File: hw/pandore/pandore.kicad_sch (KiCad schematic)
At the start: 17 parts

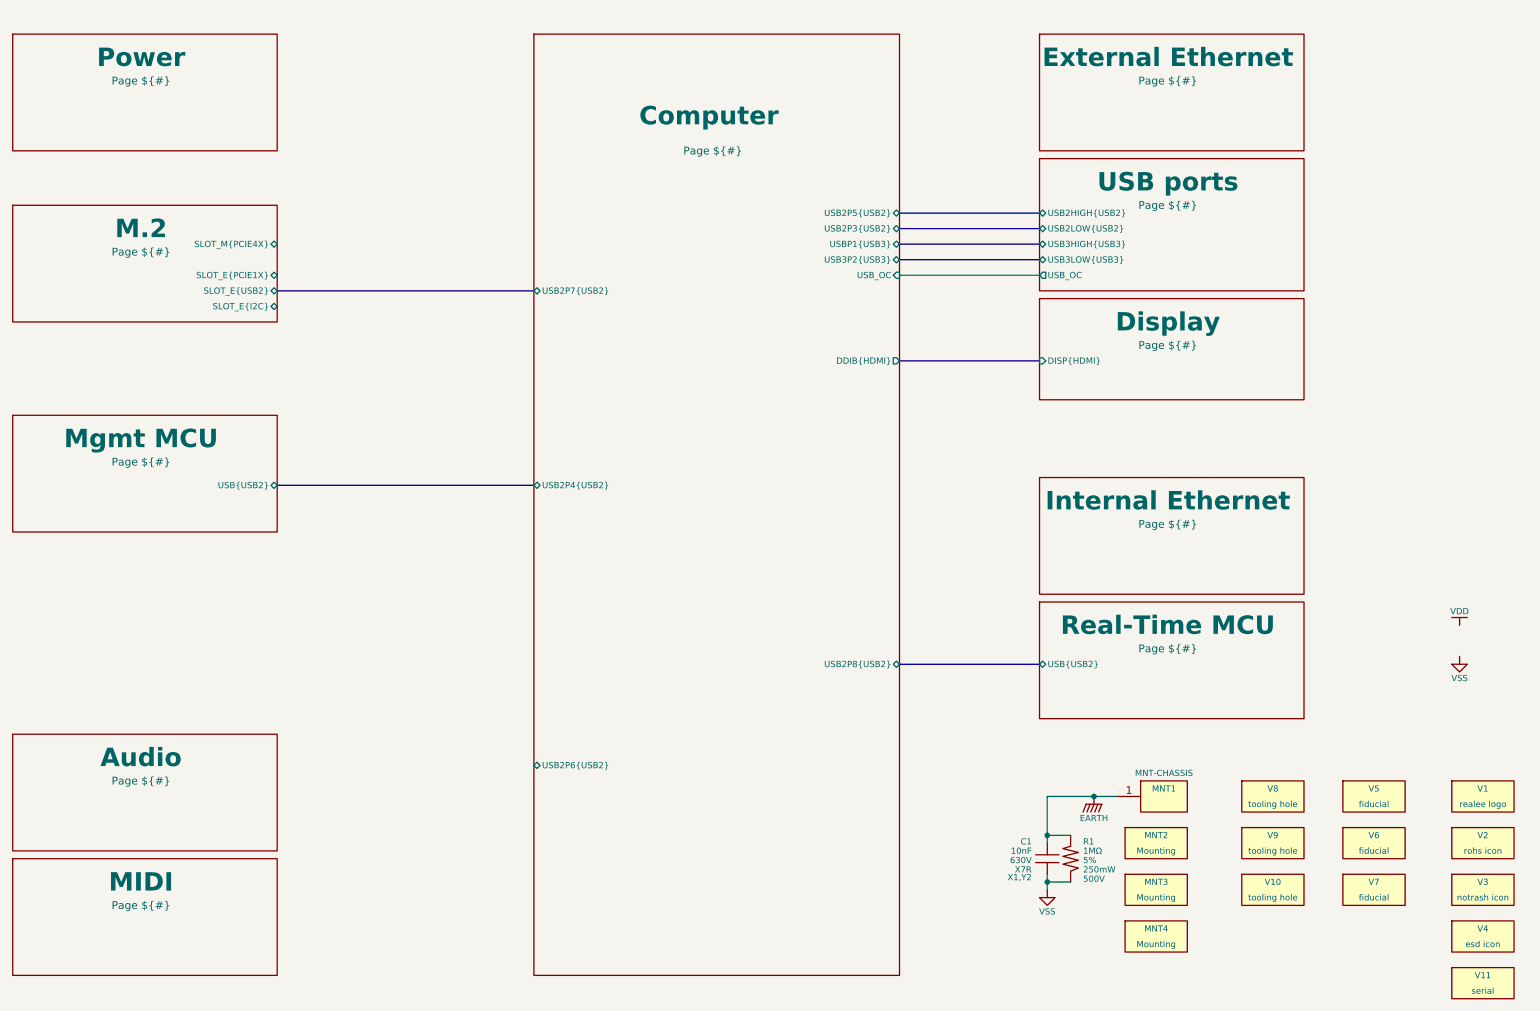
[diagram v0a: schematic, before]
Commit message: added usb, hdmi and combo xlrtrs connectors resized pcb for something realistic (still wip)
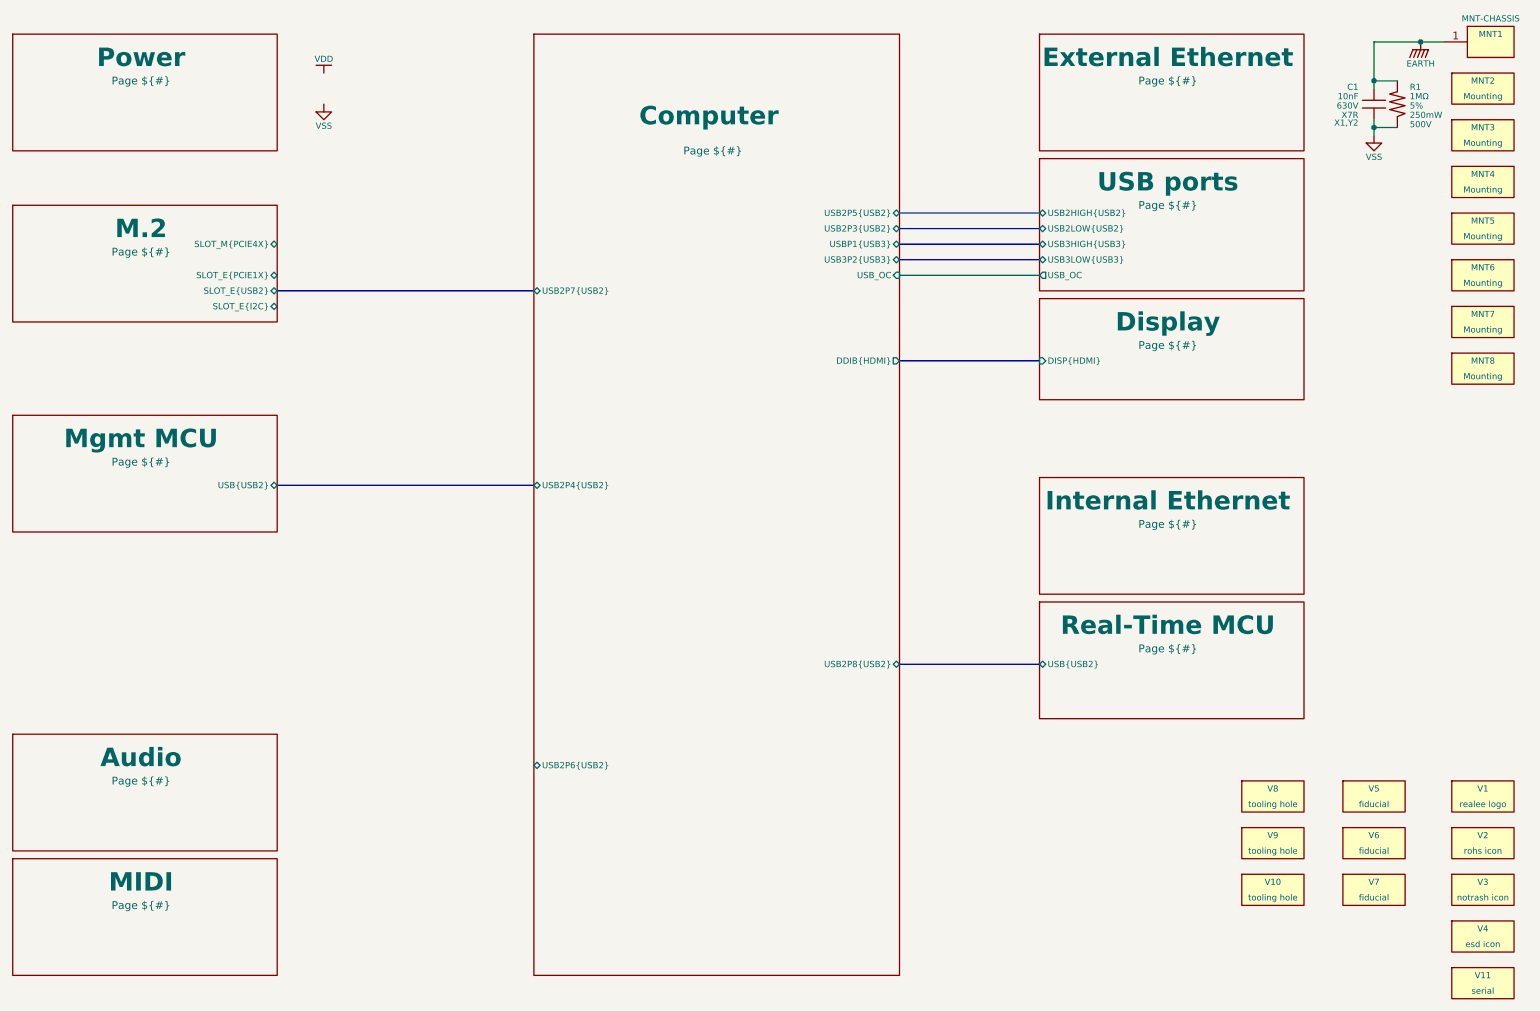
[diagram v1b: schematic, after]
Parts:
- added MNT5, MNT6, MNT7, MNT8: Mounting, reekilib_mnt:mnt_M3, symbol reekilib_vrt:virtual
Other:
- moved on the sheet: C1, MNT1, MNT2, MNT3, MNT4, R1

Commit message: Added lots to sch and pcb: eth passive, audio codec, midi, teensy Corrected and added support for M.2
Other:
- sheet Audio ports: added MIDI{UART}, USB{USB2}; removed none
- sheet Computer ports: added ETHI{PCIE1X}, ETHX{PCIE1X}, M2E{PCIE1X}, M2M{PCIE4X}, MIDI{UART}; removed none
- sheet External Ethernet ports: added PCIE{PCIE1X}; removed none
- sheet Internal Ethernet ports: added PCIE{PCIE1X}; removed none
- sheet MIDI ports: added CPU{UART}, MCU{UART}; removed none
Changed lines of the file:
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@@
 			"HSO12+" "HSO12-" "HSI12+" "HSI12-" "HSO13+" "HSO13-" "HSI13+" "HSI13-"
 			"HSO14+" "HSO14-" "HSI14+" "HSI14-" "HSO15+" "HSO15-" "HSI15+" "HSI15-"
+			"~{CLKREQ}" "SUSCLK"
 		)
 	)
@@
 		(members "~{PRSNT[1..2]}" "SMCLK" "SMDAT" "~{TRST}" "TCK" "TDI" "TDO" "TMS"
 			"~{PERST}" "~{WAKE}" "REFCLK+" "REFCLK-" "HSO0+" "HSO0-" "HSI0+" "HSI0-"
+			"SUSCLK" "~{CLKREQ}"
 		)
 	)
@@
 			"~{PERST}" "~{WAKE}" "REFCLK+" "REFCLK-" "HSO0+" "HSO0-" "HSI0+" "HSI0-"
 			"HSO1+" "HSO1-" "HSI1+" "HSI1-" "HSO2+" "HSO2-" "HSI2+" "HSI2-" "HSO3+"
-			"HSO3-" "HSI3+" "HSI3-"
+			"HSO3-" "HSI3+" "HSI3-" "~{CLKREQ}" "SUSCLK"
 		)
 	)
@@
 			"HSO3-" "HSI3+" "HSI3-" "HSO4+" "HSO4-" "HSI4+" "HSI4-" "HSO5+" "HSO5-"
 			"HSI5+" "HSI5-" "HSO6+" "HSO6-" "HSI6+" "HSI6-" "HSO7+" "HSO7-" "HSI7+"
-			"HSI7-"
+			"HSI7-" "~{CLKREQ}" "SUSCLK"
 		)
 	)
@@
 	(bus
 		(pts
+			(xy 76.2 138.43) (xy 118.11 138.43)
+		)
+		(stroke
+			(width 0)
+			(type default)
+		)
+	)
+	(bus
+		(pts
+			(xy 78.74 149.86) (xy 78.74 162.56)
+		)
+		(stroke
+			(width 0)
+			(type default)
+		)
+	)
+	(bus
+		(pts
 			(xy 177.8 50.8) (xy 200.66 50.8)
 		)
@@
 	(bus
 		(pts
+			(xy 78.74 162.56) (xy 76.2 162.56)
+		)
+		(stroke
+			(width 0)
+			(type default)
+		)
+	)
+	(bus
+		(pts
 			(xy 177.8 53.34) (xy 200.66 53.34)
 		)
@@
 		)
 	)
+	(bus
+		(pts
+			(xy 76.2 165.1) (xy 118.11 165.1)
+		)
+		(stroke
+			(width 0)
+			(type default)
+		)
+	)
+	(bus
+		(pts
+			(xy 76.2 58.42) (xy 118.11 58.42)
+		)
+		(stroke
+			(width 0)
+			(type default)
+		)
+	)
 	(wire
 		(pts
@@
 		)
 	)
+	(bus
+		(pts
+			(xy 177.8 34.29) (xy 200.66 34.29)
+		)
+		(stroke
+			(width 0)
+			(type default)
+		)
+	)
 	(wire
 		(pts
@@
 		)
 	)
+	(bus
+		(pts
+			(xy 177.8 106.68) (xy 200.66 106.68)
+		)
+		(stroke
+			(width 0)
+			(type default)
+		)
+	)
 	(wire
 		(pts
@@
 		)
 	)
+	(bus
+		(pts
+			(xy 76.2 53.34) (xy 118.11 53.34)
+		)
+		(stroke
+			(width 0)
+			(type default)
+		)
+	)
+	(bus
+		(pts
+			(xy 76.2 149.86) (xy 78.74 149.86)
+		)
+		(stroke
+			(width 0)
+			(type default)
+		)
+	)
 	(netclass_flag ""
 		(length 1.27)
@@
 			)
 		)
+		(pin "MCU{UART}" bidirectional
+			(at 76.2 162.56 0)
+			(effects
+				(font
+					(size 1.016 1.016)
+				)
+				(justify right)
+			)
+		)
+		(pin "CPU{UART}" bidirectional
+			(at 76.2 165.1 0)
+			(effects
+				(font
+					(size 1.016 1.016)
+				)
+				(justify right)
+			)
+		)
 		(instances
 			(project "pandore"
@@
 			)
 		)
+		(pin "PCIE{PCIE1X}" bidirectional
+			(at 200.66 106.68 180)
+			(effects
+				(font
+					(size 1.016 1.016)
+				)
+				(justify left)
+			)
+		)
 		(instances
 			(project "pandore"
@@
 			)
 		)
+		(pin "ETHI{PCIE1X}" bidirectional
+			(at 177.8 106.68 0)
+			(effects
+				(font
+					(size 1.016 1.016)
+				)
+				(justify right)
+			)
+		)
+		(pin "M2M{PCIE4X}" bidirectional
+			(at 118.11 53.34 180)
+			(effects
+				(font
+					(size 1.016 1.016)
+				)
+				(justify left)
+			)
+		)
+		(pin "ETHX{PCIE1X}" bidirectional
+			(at 177.8 34.29 0)
+			(effects
+				(font
+					(size 1.016 1.016)
+				)
+				(justify right)
+			)
+		)
+		(pin "M2E{PCIE1X}" bidirectional
+			(at 118.11 58.42 180)
+			(effects
+				(font
+					(size 1.016 1.016)
+				)
+				(justify left)
+			)
+		)
+		(pin "MIDI{UART}" bidirectional
+			(at 118.11 165.1 180)
+			(effects
+				(font
+					(size 1.016 1.016)
+				)
+				(justify left)
+			)
+		)
 		(instances
 			(project "pandore"
@@
 			)
 		)
+		(pin "USB{USB2}" bidirectional
+			(at 76.2 138.43 0)
+			(effects
+				(font
+					(size 1.016 1.016)
+				)
+				(justify right)
+			)
+		)
+		(pin "MIDI{UART}" bidirectional
+			(at 76.2 149.86 0)
+			(effects
+				(font
+					(size 1.016 1.016)
+				)
+				(justify right)
+			)
+		)
 		(instances
 			(project "pandore"
@@
 			)
 		)
+		(pin "PCIE{PCIE1X}" bidirectional
+			(at 200.66 34.29 180)
+			(effects
+				(font
+					(size 1.016 1.016)
+				)
+				(justify left)
+			)
+		)

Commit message: added power stuff revised M.2 for higher model and added m.2 mounts added power tap terminals
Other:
- sheet Audio ports: added CPU{I2S1DPX}; removed none
- sheet Computer ports: added AUDIO.I2S{I2S1DPX}, AUDIO.MIDI{UART}, AUDIO.USB{USB2}; removed MIDI{UART}, USB2P6{USB2}
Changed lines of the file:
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@@
 	(bus
 		(pts
+			(xy 76.2 140.97) (xy 118.11 140.97)
+		)
+		(stroke
+			(width 0)
+			(type default)
+		)
+	)
+	(bus
+		(pts
 			(xy 76.2 138.43) (xy 118.11 138.43)
 		)
@@
 			)
 		)
-		(pin "USB2P6{USB2}" bidirectional
-			(at 118.11 138.43 180)
-			(effects
-				(font
-					(size 1.016 1.016)
-				)
-				(justify left)
-			)
-		)
 		(pin "USB2P8{USB2}" bidirectional
 			(at 177.8 121.92 0)
@@
 			)
 		)
-		(pin "MIDI{UART}" bidirectional
+		(pin "AUDIO.MIDI{UART}" bidirectional
 			(at 118.11 165.1 180)
 			(effects
@@
 			)
 		)
+		(pin "AUDIO.USB{USB2}" bidirectional
+			(at 118.11 138.43 180)
+			(effects
+				(font
+					(size 1.016 1.016)
+				)
+				(justify left)
+			)
+		)
+		(pin "AUDIO.I2S{I2S1DPX}" bidirectional
+			(at 118.11 140.97 180)
+			(effects
+				(font
+					(size 1.016 1.016)
+				)
+				(justify left)
+			)
+		)
 		(instances
 			(project "pandore"
@@
 			(effects
 				(font
+					(size 1.016 1.016)
+				)
+				(justify right)
+			)
+		)
+		(pin "CPU{I2S1DPX}" bidirectional
+			(at 76.2 140.97 0)
+			(effects
+				(font

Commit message: added i2s/i2c isolation for audio section
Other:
- sheet Audio ports: added CPU{I2S1DPX ~{RST}}; removed CPU{I2S1DPX}
- sheet Computer ports: added AUDIO.I2S{I2S1DPX ~{RST}}; removed AUDIO.I2S{I2S1DPX}
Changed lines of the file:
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@@
 			)
 		)
-		(pin "AUDIO.I2S{I2S1DPX}" bidirectional
+		(pin "AUDIO.I2S{I2S1DPX ~{RST}}" bidirectional
 			(at 118.11 140.97 180)
 			(effects
@@
 			)
 		)
-		(pin "CPU{I2S1DPX}" bidirectional
+		(pin "CPU{I2S1DPX ~{RST}}" bidirectional
 			(at 76.2 140.97 0)
 			(effects

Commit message: lots of routing (diff, buses, power) done optimised buffer out
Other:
- sheet Audio ports: added AUDMST{I2C}; removed none
- sheet Computer ports: added AUDIO{I2C}, M2E{I2C}; removed none
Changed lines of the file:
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@@
 	(bus
 		(pts
+			(xy 76.2 63.5) (xy 118.11 63.5)
+		)
+		(stroke
+			(width 0)
+			(type default)
+		)
+	)
+	(bus
+		(pts
 			(xy 76.2 60.96) (xy 118.11 60.96)
 		)
@@
 	(bus
 		(pts
+			(xy 76.2 143.51) (xy 118.11 143.51)
+		)
+		(stroke
+			(width 0)
+			(type default)
+		)
+	)
+	(bus
+		(pts
 			(xy 177.8 34.29) (xy 200.66 34.29)
 		)
@@
 		)
 		(pin "USB2P8{USB2}" bidirectional
-			(at 177.8 121.92 0)
+			(at 118.11 92.71 180)
 			(effects
 				(font
 					(size 1.016 1.016)
 				)
-				(justify right)
+				(justify left)
 			)
 		)
@@
 		)
 		(pin "USB2P4{USB2}" bidirectional
-			(at 118.11 92.71 180)
+			(at 177.8 121.92 0)
 			(effects
 				(font
 					(size 1.016 1.016)
 				)
-				(justify left)
+				(justify right)
 			)
 		)
@@
 			)
 		)
+		(pin "AUDIO{I2C}" bidirectional
+			(at 118.11 143.51 180)
+			(effects
+				(font
+					(size 1.016 1.016)
+				)
+				(justify left)
+			)
+		)
+		(pin "M2E{I2C}" bidirectional
+			(at 118.11 63.5 180)
+			(effects
+				(font
+					(size 1.016 1.016)
+				)
+				(justify left)
+			)
+		)
 		(instances
 			(project "pandore"
@@
 			(effects
 				(font
+					(size 1.016 1.016)
+				)
+				(justify right)
+			)
+		)
+		(pin "AUDMST{I2C}" bidirectional
+			(at 76.2 143.51 0)
+			(effects
+				(font

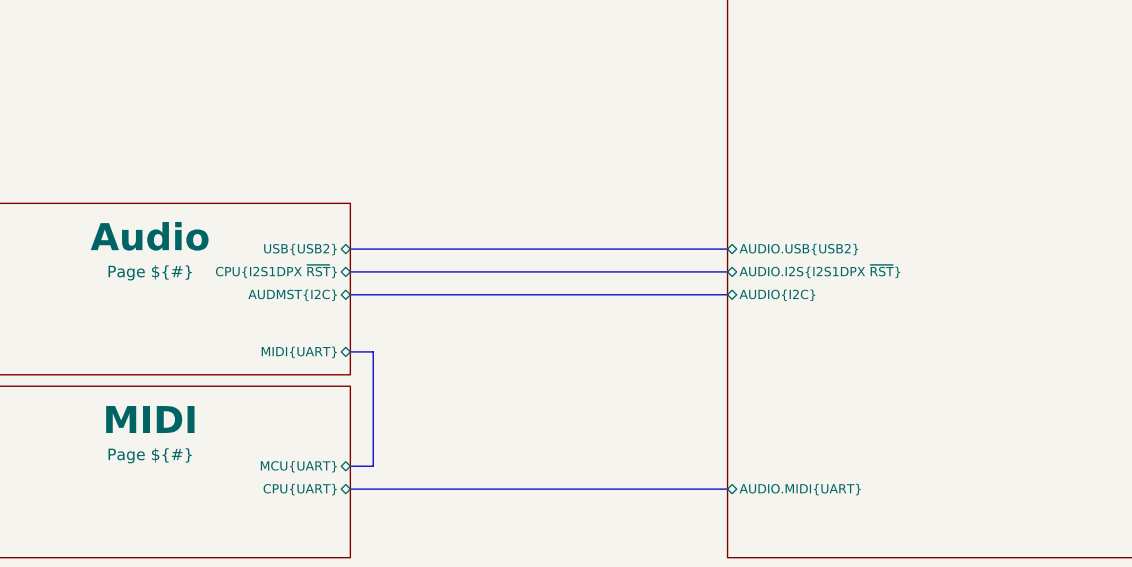
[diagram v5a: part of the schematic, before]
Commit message: lcd control circuit added fan interface added rgba output pinout for management mcu accessories done
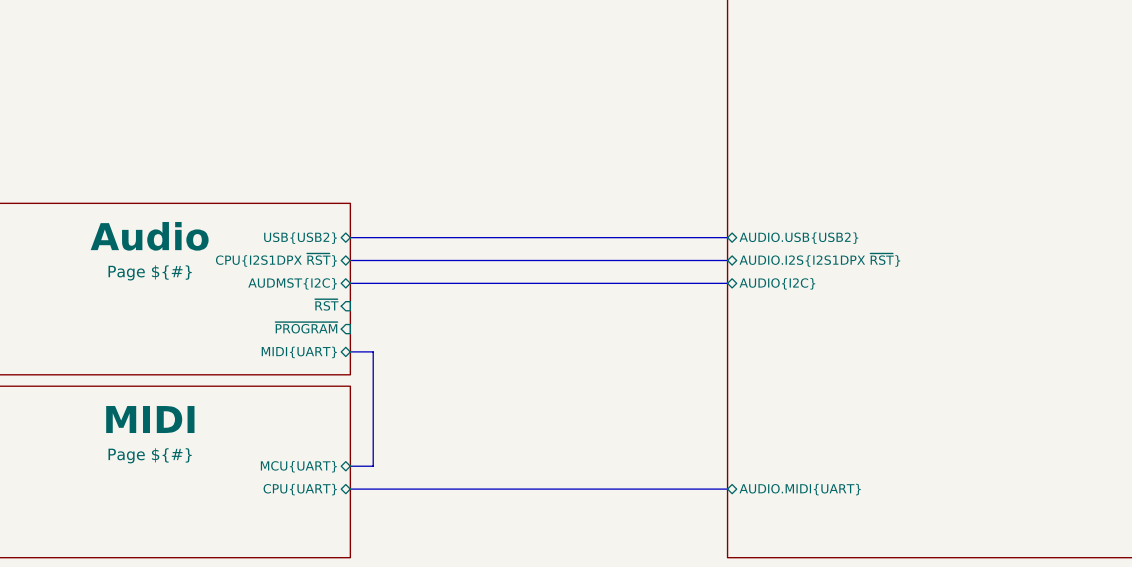
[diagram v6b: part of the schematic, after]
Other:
- sheet Audio ports: added ~{PROGRAM}, ~{RST}; removed none
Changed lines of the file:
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@@
 	(bus
 		(pts
-			(xy 76.2 140.97) (xy 118.11 140.97)
+			(xy 76.2 139.7) (xy 118.11 139.7)
 		)
 		(stroke
@@
 	(bus
 		(pts
-			(xy 76.2 138.43) (xy 118.11 138.43)
+			(xy 76.2 137.16) (xy 118.11 137.16)
 		)
 		(stroke
@@
 	(bus
 		(pts
-			(xy 76.2 143.51) (xy 118.11 143.51)
+			(xy 76.2 142.24) (xy 118.11 142.24)
 		)
 		(stroke
@@
 		)
 		(pin "AUDIO.USB{USB2}" bidirectional
-			(at 118.11 138.43 180)
+			(at 118.11 137.16 180)
 			(effects
 				(font
@@
 		)
 		(pin "AUDIO.I2S{I2S1DPX ~{RST}}" bidirectional
-			(at 118.11 140.97 180)
+			(at 118.11 139.7 180)
 			(effects
 				(font
@@
 		)
 		(pin "AUDIO{I2C}" bidirectional
-			(at 118.11 143.51 180)
+			(at 118.11 142.24 180)
 			(effects
 				(font
@@
 		)
 		(pin "USB{USB2}" bidirectional
-			(at 76.2 138.43 0)
+			(at 76.2 137.16 0)
 			(effects
 				(font
@@
 		)
 		(pin "CPU{I2S1DPX ~{RST}}" bidirectional
-			(at 76.2 140.97 0)
+			(at 76.2 139.7 0)
 			(effects
 				(font
@@
 		)
 		(pin "AUDMST{I2C}" bidirectional
-			(at 76.2 143.51 0)
+			(at 76.2 142.24 0)
+			(effects
+				(font
+					(size 1.016 1.016)
+				)
+				(justify right)
+			)
+		)
+		(pin "~{RST}" input
+			(at 76.2 144.78 0)
+			(effects
+				(font
+					(size 1.016 1.016)
+				)
+				(justify right)
+			)
+		)
+		(pin "~{PROGRAM}" input
+			(at 76.2 147.32 0)
 			(effects
 				(font
